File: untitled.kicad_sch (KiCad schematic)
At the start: 30 parts, among them J10 IN 1x6h, J11 SYNC, J12 PWM, J13 CV, J14 1VOct, J15 FM, J17 OCT_SW 1x7h, J19 CV 1x6h, J21 CTRL 1x9h, J3 OUT 1x4h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

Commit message: Added +5v ref supply
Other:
- moved on the sheet: H5, H6, H7, H8
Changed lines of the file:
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@@
 	(symbol
 		(lib_id "Mechanical:MountingHole")
-		(at 21.59 189.23 0)
+		(at 27.94 189.23 0)
 		(unit 1)
 		(exclude_from_sim no)
@@
 		(fields_autoplaced yes)
 		(property "Reference" "H8"
-			(at 24.13 187.9599 0)
+			(at 30.48 187.9599 0)
 			(effects
 				(font
@@
 		)
 		(property "Value" "~"
-			(at 24.13 190.4999 0)
+			(at 30.48 190.4999 0)
 			(effects
 				(font
@@
 		)
 		(property "Footprint" "MountingHole:MountingHole_2.7mm_M2.5"
-			(at 21.59 189.23 0)
+			(at 27.94 189.23 0)
 			(effects
 				(font
@@
 		)
 		(property "Datasheet" "~"
-			(at 21.59 189.23 0)
+			(at 27.94 189.23 0)
 			(effects
 				(font
@@
 		)
 		(property "Description" "Mounting Hole without connection"
-			(at 21.59 189.23 0)
+			(at 27.94 189.23 0)
 			(effects
 				(font
@@
 	(symbol
 		(lib_id "Mechanical:MountingHole")
-		(at 21.59 173.99 0)
+		(at 27.94 173.99 0)
 		(unit 1)
 		(exclude_from_sim no)
@@
 		(fields_autoplaced yes)
 		(property "Reference" "H5"
-			(at 24.13 172.7199 0)
+			(at 30.48 172.7199 0)
 			(effects
 				(font
@@
 		)
 		(property "Value" "~"
-			(at 24.13 175.2599 0)
+			(at 30.48 175.2599 0)
 			(effects
 				(font
@@
 		)
 		(property "Footprint" "MountingHole:MountingHole_2.7mm_M2.5"
-			(at 21.59 173.99 0)
+			(at 27.94 173.99 0)
 			(effects
 				(font
@@
 		)
 		(property "Datasheet" "~"
-			(at 21.59 173.99 0)
+			(at 27.94 173.99 0)
 			(effects
 				(font
@@
 		)
 		(property "Description" "Mounting Hole without connection"
-			(at 21.59 173.99 0)
+			(at 27.94 173.99 0)
 			(effects
 				(font
@@
 	(symbol
 		(lib_id "Mechanical:MountingHole")
-		(at 21.59 184.15 0)
+		(at 27.94 184.15 0)
 		(unit 1)
 		(exclude_from_sim no)
@@
 		(fields_autoplaced yes)
 		(property "Reference" "H7"
-			(at 24.13 182.8799 0)
+			(at 30.48 182.8799 0)
 			(effects
 				(font
@@
 		)
 		(property "Value" "~"
-			(at 24.13 185.4199 0)
+			(at 30.48 185.4199 0)
 			(effects
 				(font
@@
 		)
 		(property "Footprint" "MountingHole:MountingHole_2.7mm_M2.5"
-			(at 21.59 184.15 0)
+			(at 27.94 184.15 0)
 			(effects
 				(font
@@
 		)
 		(property "Datasheet" "~"
-			(at 21.59 184.15 0)
+			(at 27.94 184.15 0)
 			(effects
 				(font
@@
 		)
 		(property "Description" "Mounting Hole without connection"
-			(at 21.59 184.15 0)
+			(at 27.94 184.15 0)
 			(effects
 				(font
@@
 	(symbol
 		(lib_id "Mechanical:MountingHole")
-		(at 21.59 179.07 0)
+		(at 27.94 179.07 0)
 		(unit 1)
 		(exclude_from_sim no)
@@
 		(fields_autoplaced yes)
 		(property "Reference" "H6"
-			(at 24.13 177.7999 0)
+			(at 30.48 177.7999 0)
 			(effects
 				(font
@@
 		)
 		(property "Value" "~"
-			(at 24.13 180.3399 0)
+			(at 30.48 180.3399 0)
 			(effects
 				(font
@@
 		)
 		(property "Footprint" "MountingHole:MountingHole_2.7mm_M2.5"
-			(at 21.59 179.07 0)
+			(at 27.94 179.07 0)
 			(effects
 				(font
@@
 		)
 		(property "Datasheet" "~"
-			(at 21.59 179.07 0)
+			(at 27.94 179.07 0)
 			(effects
 				(font
@@
 		)
 		(property "Description" "Mounting Hole without connection"
-			(at 21.59 179.07 0)
-			(effects
-				(font
+			(at 27.94 179.07 0)
+			(effects
+				(font

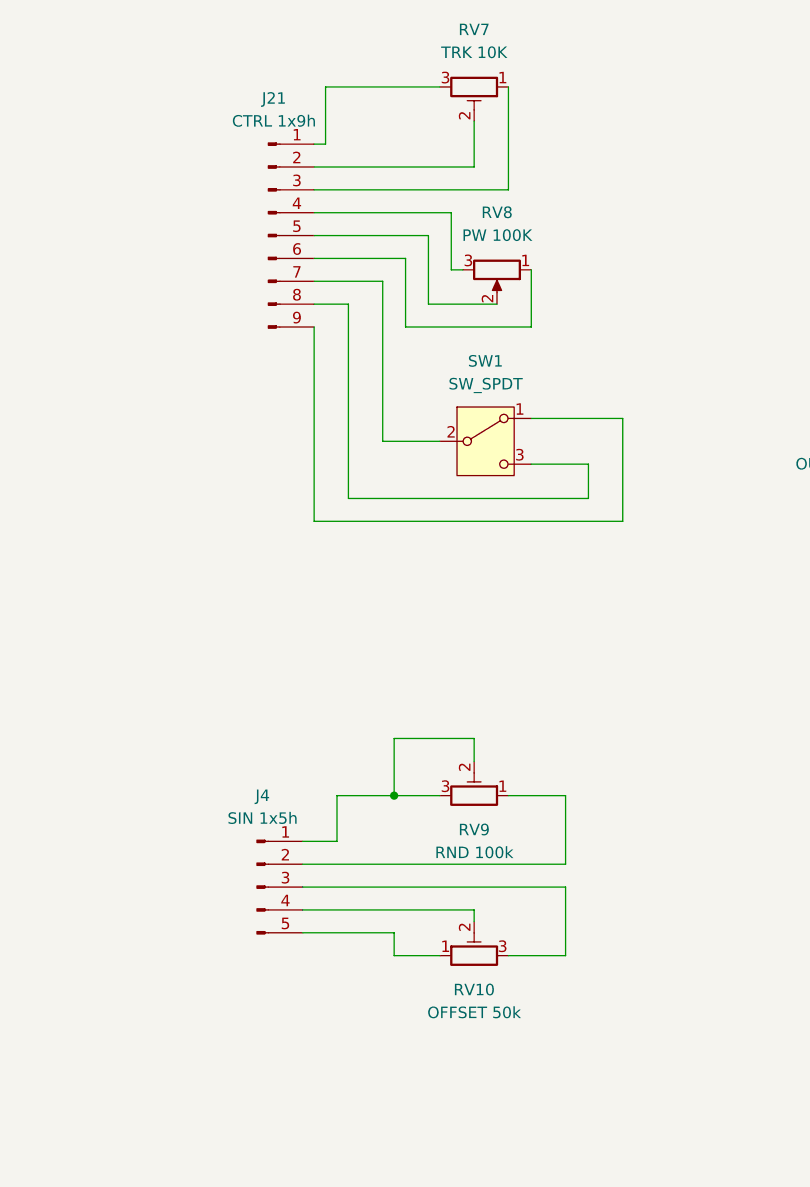
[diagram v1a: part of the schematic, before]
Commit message: +5V ref update
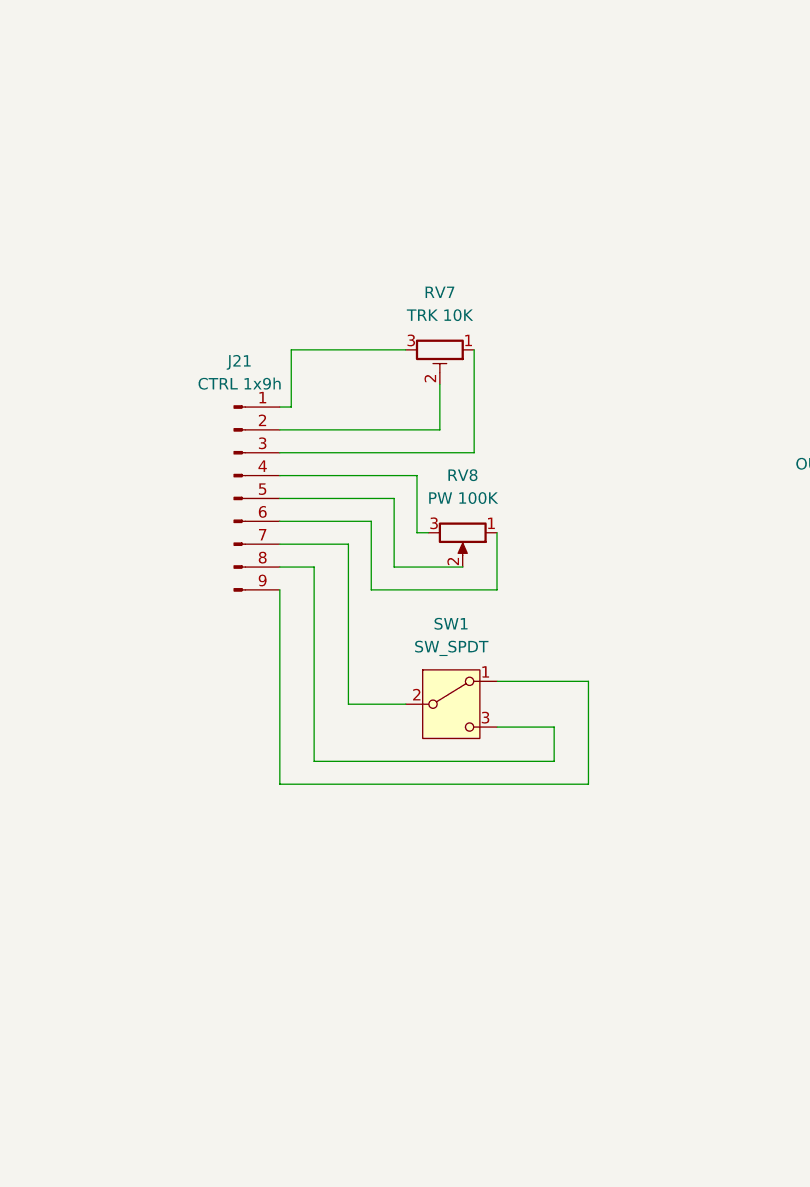
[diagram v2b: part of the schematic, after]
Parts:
- removed J4: SIN 1x5h, Connector_PinHeader_2.54mm:PinHeader_1x05_P2.54mm_Vertical, symbol Connector:Conn_01x05_Pin
- removed RV10: OFFSET 50k, Potentiometer_THT:Potentiometer_Bourns_3296W_Vertical, symbol Device:R_Potentiometer_Trim
- removed RV9: RND 100k, Potentiometer_THT:Potentiometer_Bourns_3296W_Vertical, symbol Device:R_Potentiometer_Trim
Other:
- moved on the sheet: J21, RV7, RV8, SW1

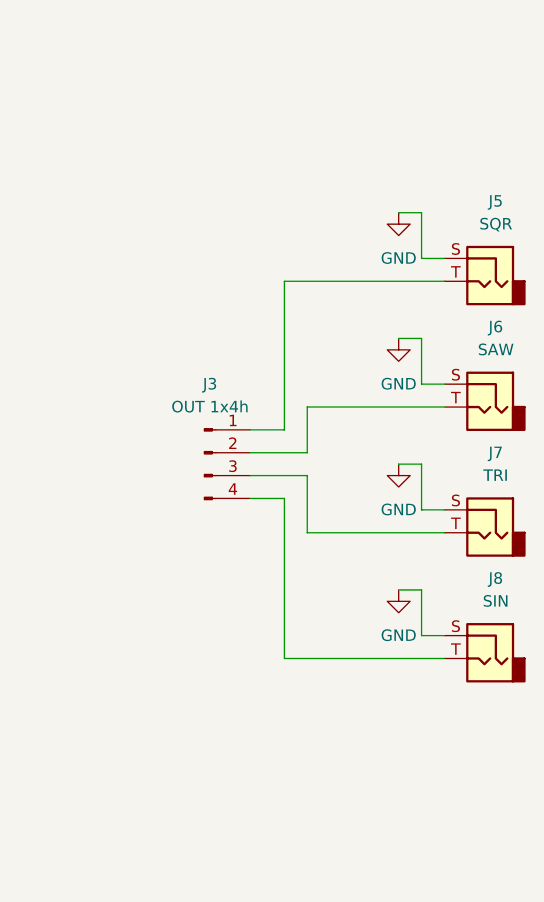
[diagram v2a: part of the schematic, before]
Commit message: Corrected output jack sockets
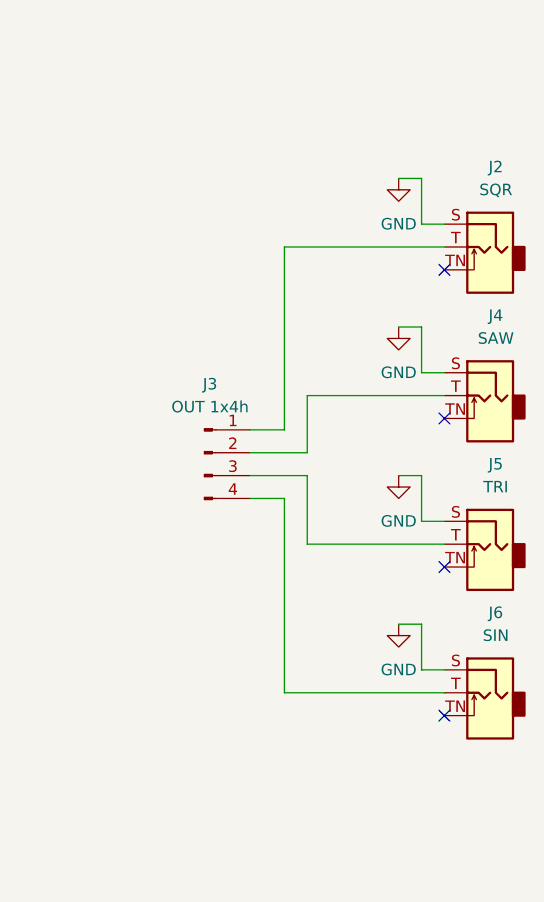
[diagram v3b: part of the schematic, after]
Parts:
- removed J5: SQR, Connector_Audio:Jack_3.5mm_QingPu_WQP-PJ398SM_Vertical_CircularHoles, symbol Connector_Audio:AudioJack2
- removed J6: SAW, Connector_Audio:Jack_3.5mm_QingPu_WQP-PJ398SM_Vertical_CircularHoles, symbol Connector_Audio:AudioJack2
- removed J7: TRI, Connector_Audio:Jack_3.5mm_QingPu_WQP-PJ398SM_Vertical_CircularHoles, symbol Connector_Audio:AudioJack2
- removed J8: SIN, Connector_Audio:Jack_3.5mm_QingPu_WQP-PJ398SM_Vertical_CircularHoles, symbol Connector_Audio:AudioJack2
- added J2: SQR, Connector_Audio:Jack_3.5mm_QingPu_WQP-PJ398SM_Vertical_CircularHoles, symbol Connector_Audio:AudioJack2_SwitchT
- added J4: SAW, Connector_Audio:Jack_3.5mm_QingPu_WQP-PJ398SM_Vertical_CircularHoles, symbol Connector_Audio:AudioJack2_SwitchT
- added J5: TRI, Connector_Audio:Jack_3.5mm_QingPu_WQP-PJ398SM_Vertical_CircularHoles, symbol Connector_Audio:AudioJack2_SwitchT
- added J6: SIN, Connector_Audio:Jack_3.5mm_QingPu_WQP-PJ398SM_Vertical_CircularHoles, symbol Connector_Audio:AudioJack2_SwitchT
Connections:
- net GND: now also J2.S, J4.S, J5.S, J6.S
- net at J3.2 (Pin_2): now also J4.T
- net at J3.3 (Pin_3): now also J5.T
- net at J3.1 (Pin_1): now also J2.T
- net at J3.4 (Pin_4): now also J6.T
- no-connect marks 1 -> 5

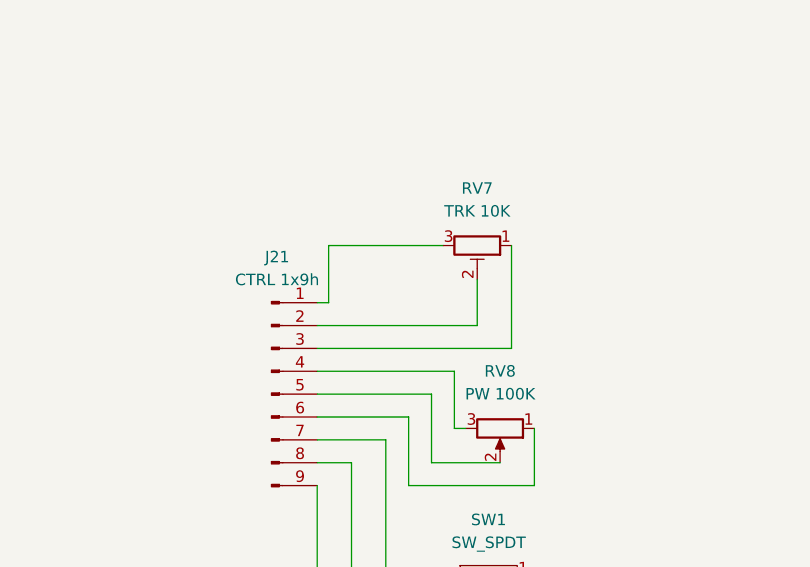
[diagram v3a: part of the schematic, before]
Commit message: Updated simulator and corrected trk pot
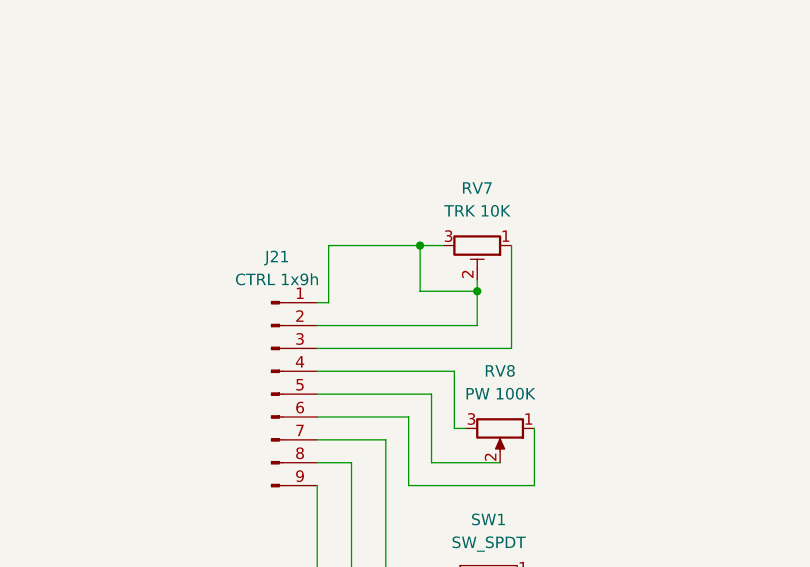
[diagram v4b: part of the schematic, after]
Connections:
- net at J21.1 (Pin_1), RV7.3: now also J21.2 (Pin_2), RV7.2
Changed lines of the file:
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@@
+	)
+	(junction
+		(at 196.85 73.66)
+		(diameter 0)
+		(color 0 0 0 0)
 	)
 	(junction
@@
 	)
 	(junction
+		(at 190.5 68.58)
+		(diameter 0)
+		(color 0 0 0 0)
+	)
+	(junction
 		(at 31.75 95.25)
 		(diameter 0)
@@
 	(wire
 		(pts
-			(xy 193.04 68.58) (xy 180.34 68.58)
+			(xy 193.04 68.58) (xy 190.5 68.58)
 		)
 		(stroke
@@
 	(wire
 		(pts
+			(xy 190.5 68.58) (xy 190.5 73.66)
+		)
+		(stroke
+			(width 0)
+			(type default)
+		)
+	)
+	(wire
+		(pts
 			(xy 266.7 93.98) (xy 264.16 93.98)
 		)
@@
 	(wire
 		(pts
+			(xy 190.5 68.58) (xy 180.34 68.58)
+		)
+		(stroke
+			(width 0)
+			(type default)
+		)
+	)
+	(wire
+		(pts
 			(xy 34.29 50.8) (xy 34.29 53.34)
 		)
@@
 	(wire
 		(pts
-			(xy 196.85 72.39) (xy 196.85 77.47)
+			(xy 196.85 72.39) (xy 196.85 73.66)
 		)
 		(stroke
@@
 	(wire
 		(pts
+			(xy 196.85 73.66) (xy 196.85 77.47)
+		)
+		(stroke
+			(width 0)
+			(type default)
+		)
+	)
+	(wire
+		(pts
 			(xy 78.74 80.01) (xy 64.77 80.01)
 		)
@@
 		)
 		(stroke
+			(width 0)
+			(type default)
+		)
+	)
+	(wire
+		(pts
+			(xy 190.5 73.66) (xy 196.85 73.66)
+		)
+		(stroke

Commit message: Updates to jacks
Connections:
- net GND: no longer J11.TN, J12.TN, J13.TN, J14.TN, J15.TN
- no-connect marks 5 -> 10
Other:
- note added: "VCO II (front panel)"

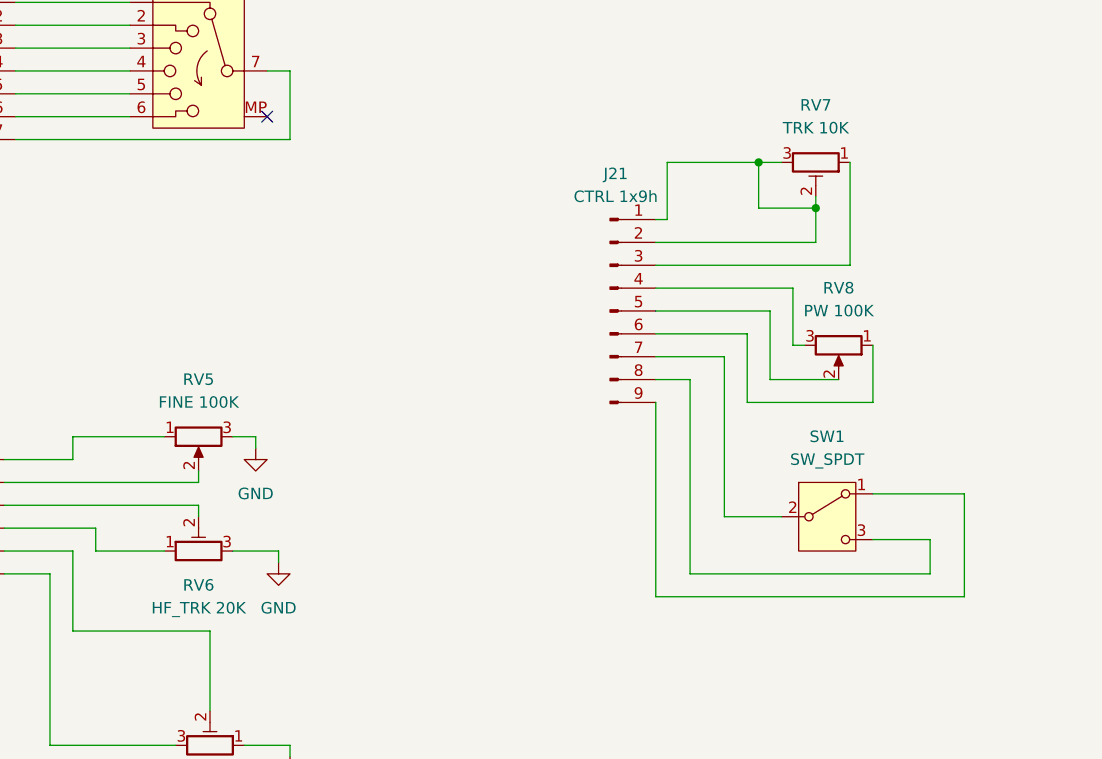
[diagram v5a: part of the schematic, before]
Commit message: Fixed FM sweep
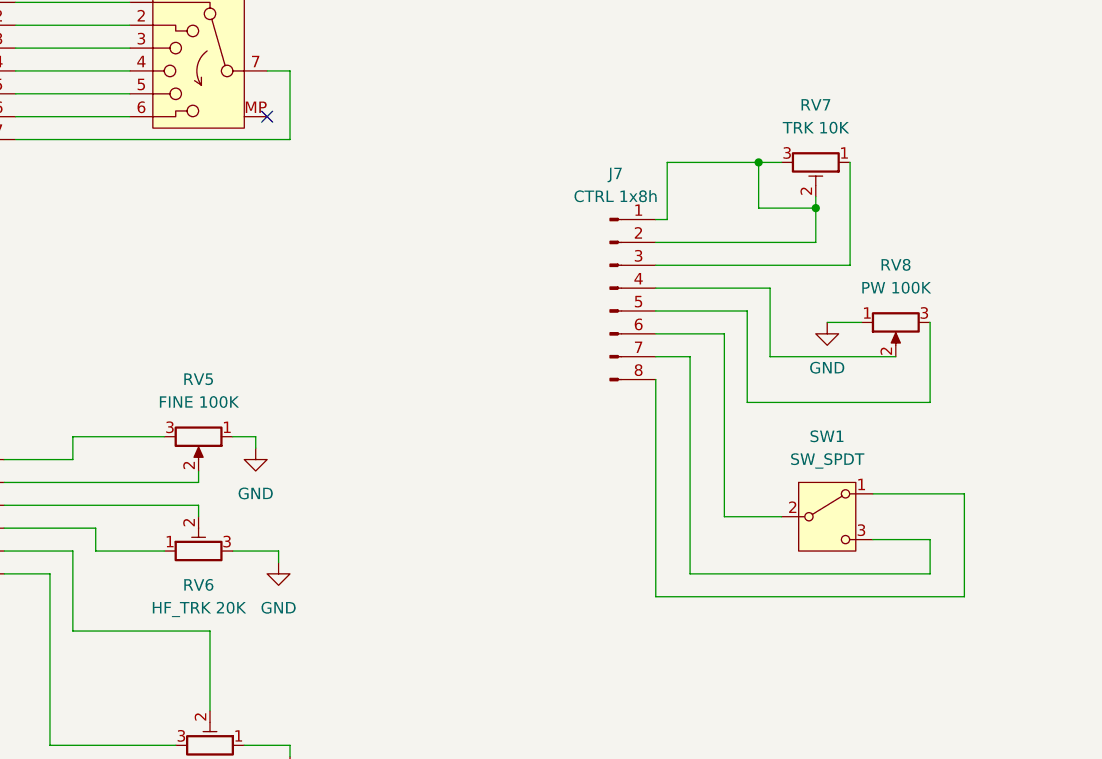
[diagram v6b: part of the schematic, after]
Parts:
- removed J21: CTRL 1x9h, Connector_PinHeader_2.54mm:PinHeader_1x08_P2.54mm_Vertical, symbol Connector:Conn_01x09_Pin
- added J7: CTRL 1x8h, symbol Connector:Conn_01x08_Pin
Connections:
- net GND: now also RV5.1, RV8.1; no longer RV5.3
- net at RV7.2, RV7.3: now also J7.1 (Pin_1), J7.2 (Pin_2)
- net at RV7.1: now also J7.3 (Pin_3)
- net at RV8.3: now also J7.5 (Pin_5)
- net at RV8.2: now also J7.4 (Pin_4)
- net at SW1.2 (B): now also J7.6 (Pin_6)
- net at SW1.3 (C): now also J7.7 (Pin_7)
- net at SW1.1 (A): now also J7.8 (Pin_8)
- net at J19.1 (Pin_1): now also RV5.3; no longer RV5.1
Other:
- moved on the sheet: RV5, RV8

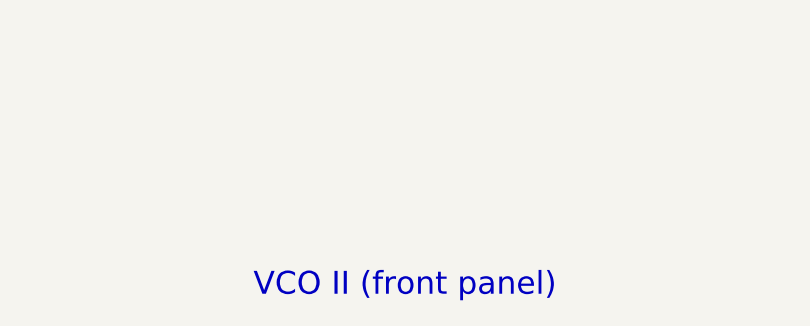
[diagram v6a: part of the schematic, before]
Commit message: Added images to read me
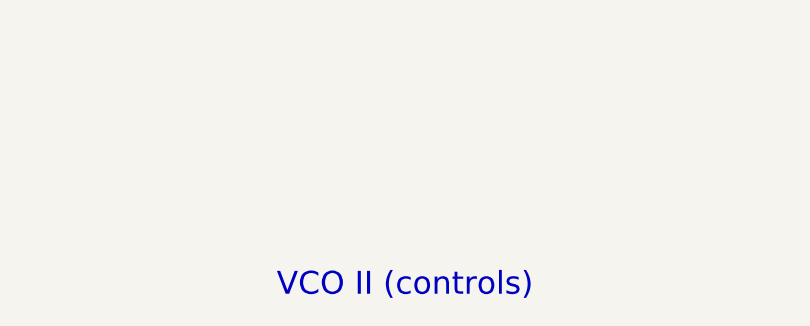
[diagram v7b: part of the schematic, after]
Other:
- note added: "VCO II (controls)"
- note removed: "VCO II (front panel)"
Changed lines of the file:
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@@
 	(generator_version "9.0")
 	(paper "A4")
-	(text "VCO II (front panel)"
+	(text "VCO II (controls)"
 		(exclude_from_sim no)
 		(at 205.74 189.738 0)
